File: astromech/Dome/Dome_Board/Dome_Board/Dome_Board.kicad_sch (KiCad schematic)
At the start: 3 parts, among them J1 Conn_01x02_Socket, J2 Conn_01x02_Socket, U1 ESP32-C6-DEVKITC-1-N8

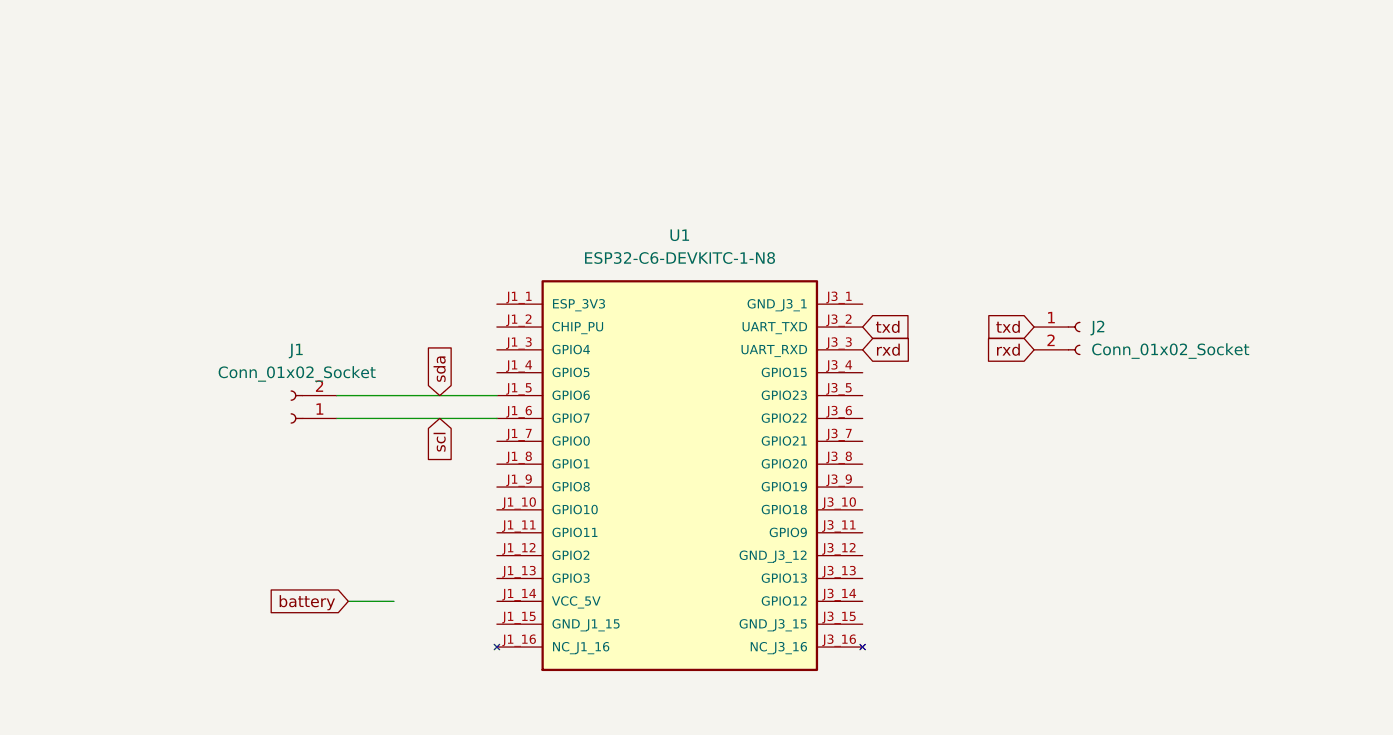
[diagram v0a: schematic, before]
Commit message: added battery 5vRegulator 10/12
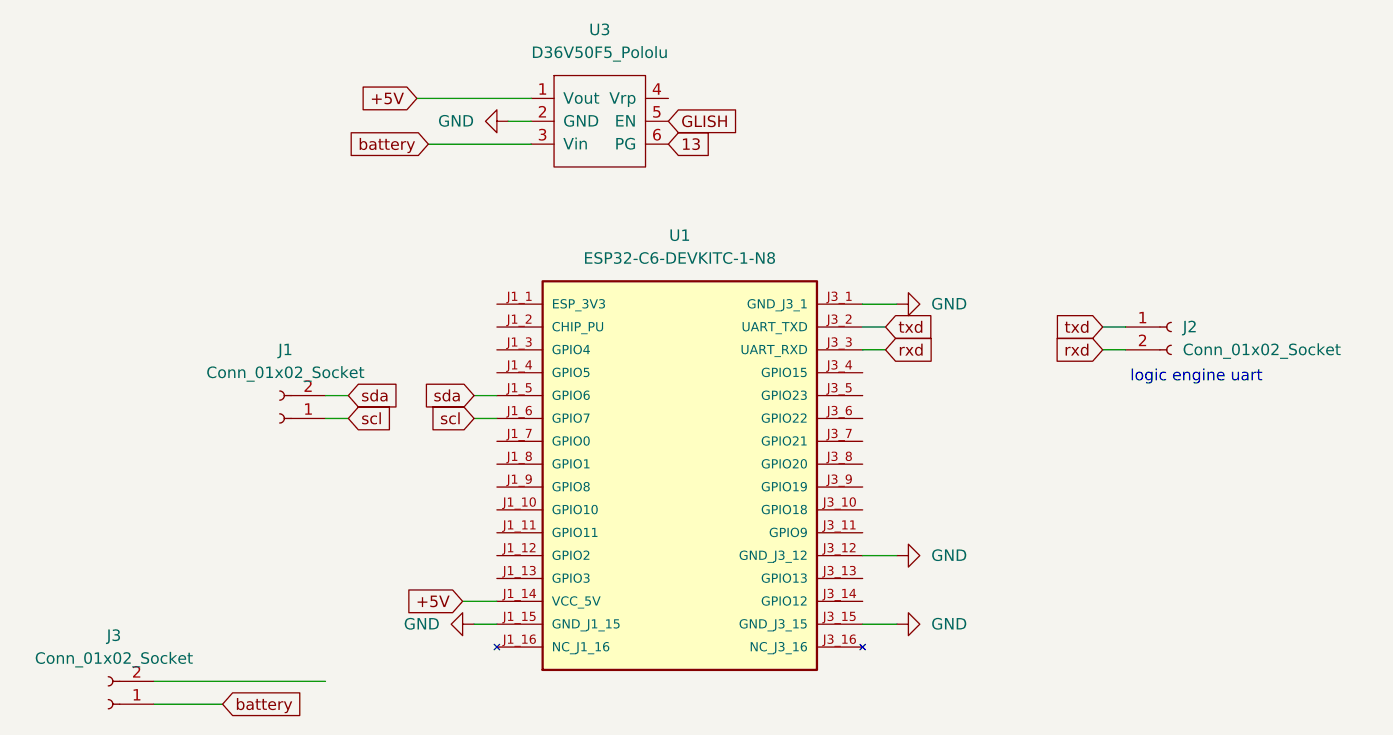
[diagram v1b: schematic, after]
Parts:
- added J3: Conn_01x02_Socket, Connector_PinSocket_1.27mm:PinSocket_1x02_P1.27mm_Vertical, symbol Connector:Conn_01x02_Socket
- added U3: D36V50F5_Pololu, js:D36V50F5_Pololu, symbol js:D36V50F5_Pololu
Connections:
- net battery: now also J3.1 (Pin_1), U3.3 (Vin)
- net +5V: now reaches U1.J1_14 (VCC_5V)
- net +5V: now also U3.1 (Vout)
- net GND: now reaches U1.J1_15 (GND_J1_15)
- net GND: now also U1.J3_1 (GND_J3_1), U1.J3_12 (GND_J3_12), U1.J3_15 (GND_J3_15), U3.2 (GND)
- new net 13: U3.6 (PG)
- new net GLISH: U3.5 (EN)
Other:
- note added: "logic engine uart"
- moved on the sheet: J1, J2

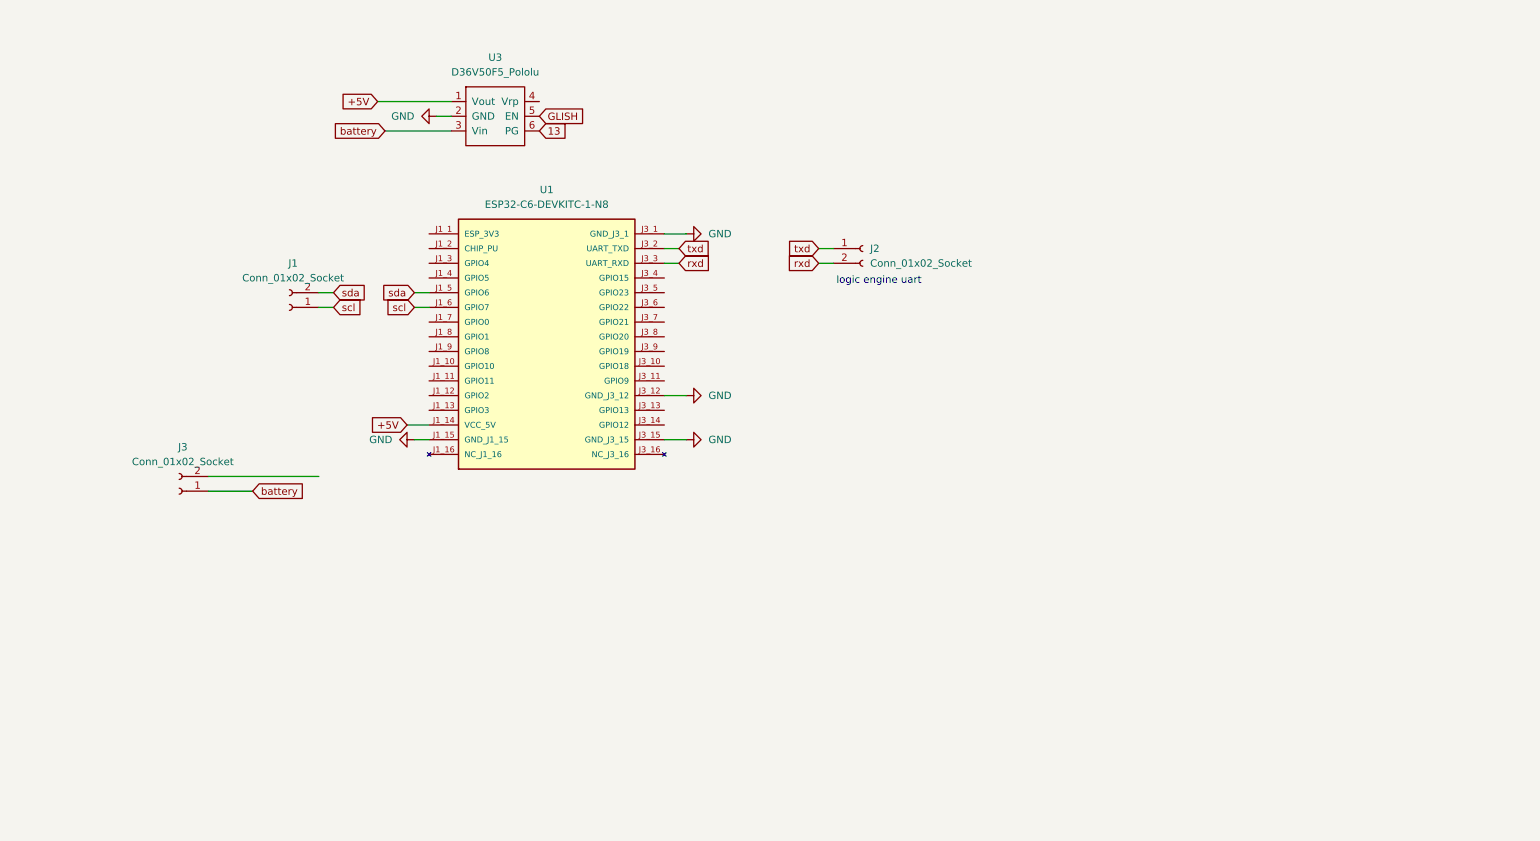
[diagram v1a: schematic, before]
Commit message: added txd lp, rxd lp, pwd connectors
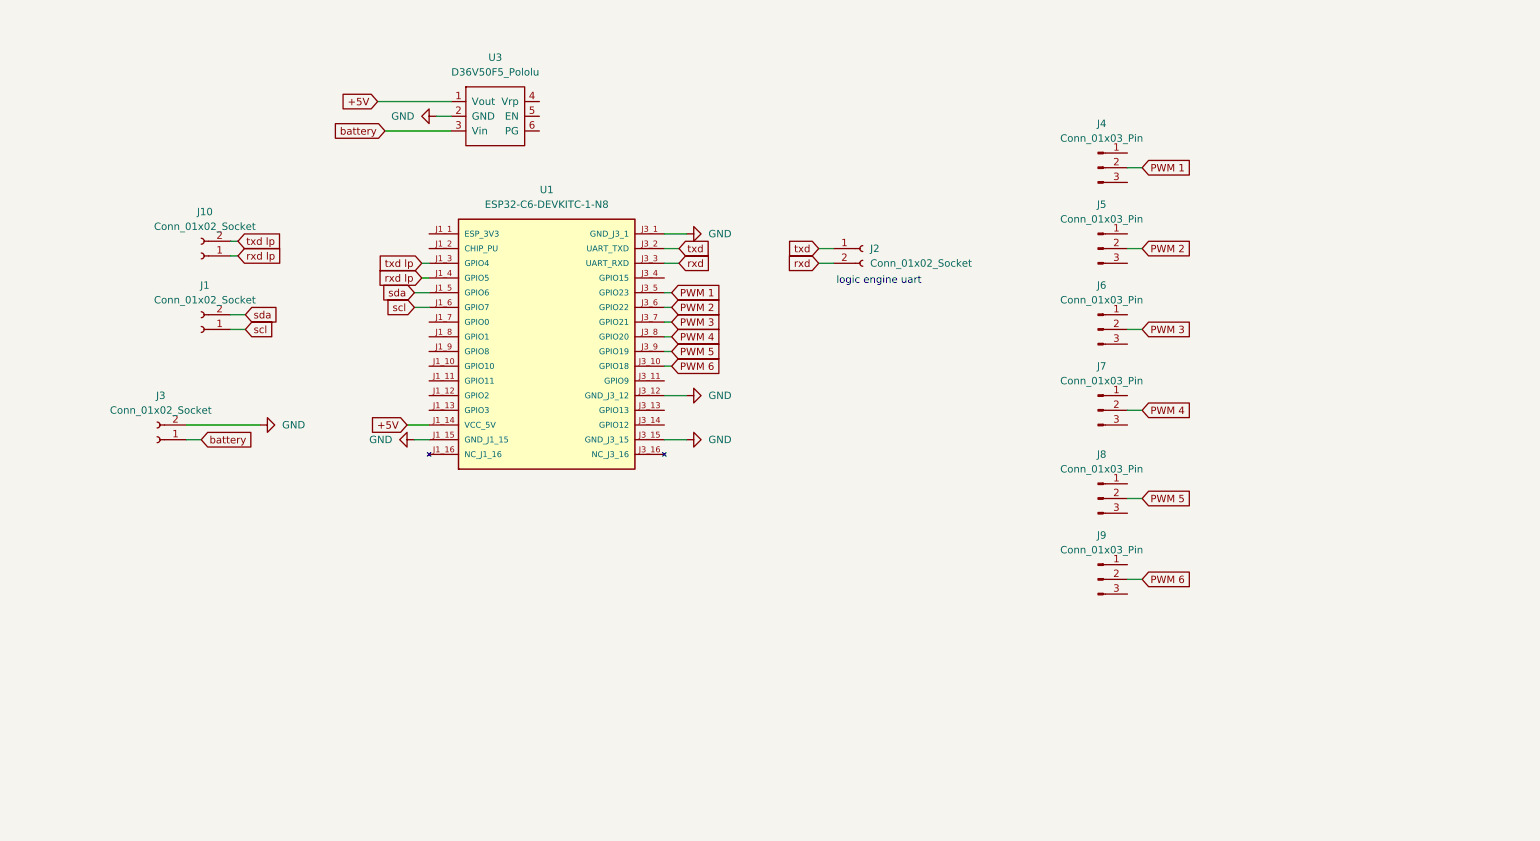
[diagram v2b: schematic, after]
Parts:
- added J10: Conn_01x02_Socket, Connector_PinSocket_1.27mm:PinSocket_1x02_P1.27mm_Vertical, symbol Connector:Conn_01x02_Socket
- added J4, J5, J6, J7, J8, J9: Conn_01x03_Pin, Connector_PinHeader_2.54mm:PinHeader_1x03_P2.54mm_Vertical, symbol Connector:Conn_01x03_Pin
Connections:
- net GND: now also J3.2 (Pin_2)
- net txd lp: now reaches U1.J1_3 (GPIO4)
- net txd lp: now also J10.2 (Pin_2)
- net rxd lp: now reaches U1.J1_4 (GPIO5)
- net rxd lp: now also J10.1 (Pin_1)
- net PWM 6: now reaches U1.J3_10 (GPIO18)
- net PWM 6: now also J9.2 (Pin_2)
- net PWM 1: now reaches U1.J3_5 (GPIO23)
- net PWM 1: now also J4.2 (Pin_2)
- net PWM 2: now reaches U1.J3_6 (GPIO22)
- net PWM 2: now also J5.2 (Pin_2)
- net PWM 3: now reaches U1.J3_7 (GPIO21)
- net PWM 3: now also J6.2 (Pin_2)
- net PWM 4: now reaches U1.J3_8 (GPIO20)
- net PWM 4: now also J7.2 (Pin_2)
- net PWM 5: now reaches U1.J3_9 (GPIO19)
- net PWM 5: now also J8.2 (Pin_2)
- net 13: no longer names the net of U3.6 (PG)
- net GLISH: no longer names the net of U3.5 (EN)
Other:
- moved on the sheet: J1, J3

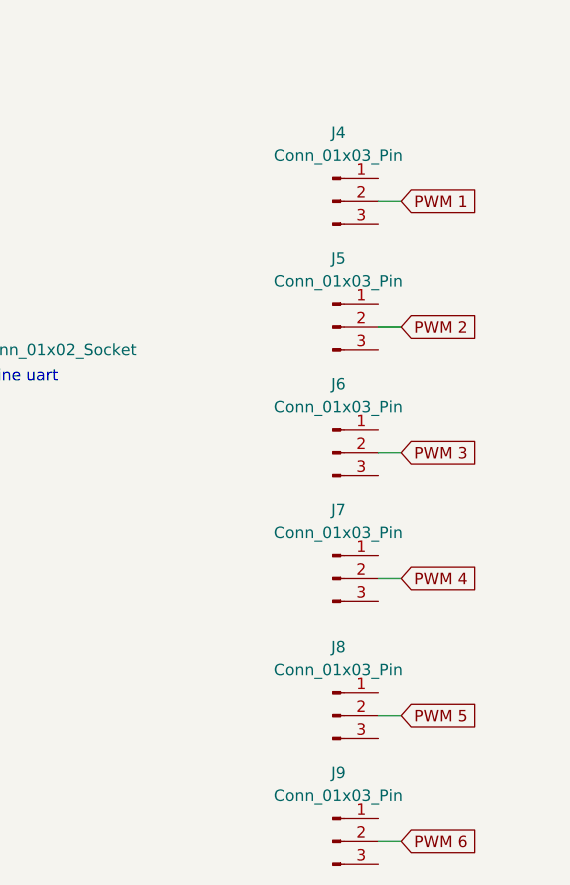
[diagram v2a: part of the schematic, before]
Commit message: added txd lp, rxd lp, PWM connectors
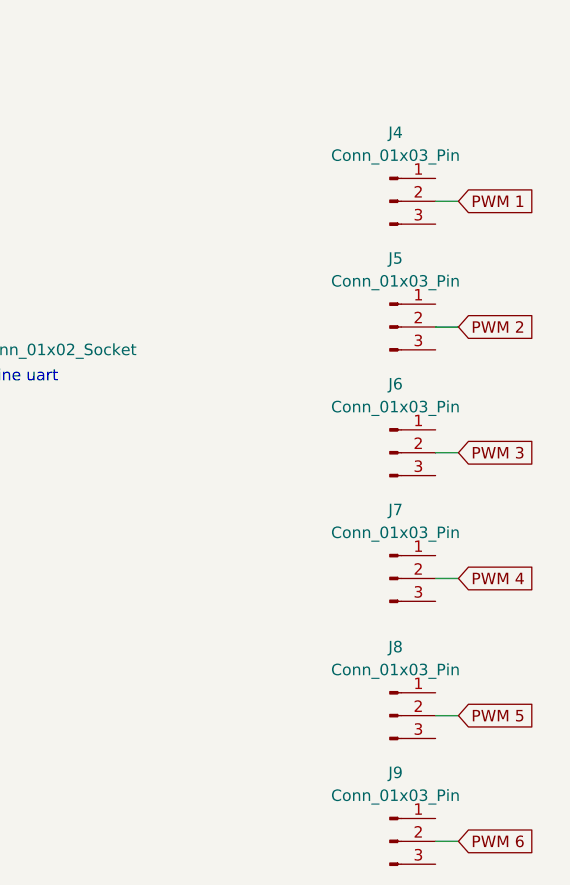
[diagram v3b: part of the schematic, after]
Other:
- moved on the sheet: J4, J5, J6, J7, J8, J9
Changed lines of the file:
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@@
 	(wire
 		(pts
-			(xy 209.55 100.33) (xy 207.01 100.33)
+			(xy 215.9 100.33) (xy 213.36 100.33)
 		)
 		(stroke
@@
 	(wire
 		(pts
-			(xy 209.55 71.12) (xy 207.01 71.12)
+			(xy 215.9 71.12) (xy 213.36 71.12)
 		)
 		(stroke
@@
 	(wire
 		(pts
-			(xy 209.55 57.15) (xy 207.01 57.15)
+			(xy 215.9 57.15) (xy 213.36 57.15)
 		)
 		(stroke
@@
 	(wire
 		(pts
-			(xy 209.55 43.18) (xy 207.01 43.18)
+			(xy 215.9 43.18) (xy 213.36 43.18)
 		)
 		(stroke
@@
 	(wire
 		(pts
-			(xy 209.55 85.09) (xy 207.01 85.09)
+			(xy 215.9 85.09) (xy 213.36 85.09)
 		)
 		(stroke
@@
 	(wire
 		(pts
-			(xy 209.55 114.3) (xy 207.01 114.3)
+			(xy 215.9 114.3) (xy 213.36 114.3)
 		)
 		(stroke
@@
 	(global_label "PWM 4"
 		(shape input)
-		(at 209.55 85.09 0)
+		(at 215.9 85.09 0)
 		(fields_autoplaced yes)
 		(effects
@@
 		)
 		(property "Intersheetrefs" "${INTERSHEET_REFS}"
-			(at 218.8851 85.09 0)
+			(at 225.2351 85.09 0)
 			(effects
 				(font
@@
 	(global_label "PWM 2"
 		(shape input)
-		(at 209.55 57.15 0)
+		(at 215.9 57.15 0)
 		(fields_autoplaced yes)
 		(effects
@@
 		)
 		(property "Intersheetrefs" "${INTERSHEET_REFS}"
-			(at 218.8851 57.15 0)
+			(at 225.2351 57.15 0)
 			(effects
 				(font
@@
 	(global_label "PWM 6"
 		(shape input)
-		(at 209.55 114.3 0)
+		(at 215.9 114.3 0)
 		(fields_autoplaced yes)
 		(effects
@@
 		)
 		(property "Intersheetrefs" "${INTERSHEET_REFS}"
-			(at 218.8851 114.3 0)
+			(at 225.2351 114.3 0)
 			(effects
 				(font
@@
 	(global_label "PWM 1"
 		(shape input)
-		(at 209.55 43.18 0)
+		(at 215.9 43.18 0)
 		(fields_autoplaced yes)
 		(effects
@@
 		)
 		(property "Intersheetrefs" "${INTERSHEET_REFS}"
-			(at 221.1228 43.18 0)
+			(at 227.4728 43.18 0)
 			(effects
 				(font
@@
 	(global_label "PWM 3"
 		(shape input)
-		(at 209.55 71.12 0)
+		(at 215.9 71.12 0)
 		(fields_autoplaced yes)
 		(effects
@@
 		)
 		(property "Intersheetrefs" "${INTERSHEET_REFS}"
-			(at 218.8851 71.12 0)
+			(at 225.2351 71.12 0)
 			(effects
 				(font
@@
 	(global_label "PWM 5"
 		(shape input)
-		(at 209.55 100.33 0)
+		(at 215.9 100.33 0)
 		(fields_autoplaced yes)
 		(effects
@@
 		)
 		(property "Intersheetrefs" "${INTERSHEET_REFS}"
-			(at 218.8851 100.33 0)
+			(at 225.2351 100.33 0)
 			(effects
 				(font
@@
 	(symbol
 		(lib_id "Connector:Conn_01x03_Pin")
-		(at 201.93 57.15 0)
+		(at 208.28 57.15 0)
 		(unit 1)
 		(exclude_from_sim no)
@@
 		(fields_autoplaced yes)
 		(property "Reference" "J5"
-			(at 202.565 49.53 0)
+			(at 208.915 49.53 0)
 			(effects
 				(font
@@
 		)
 		(property "Value" "Conn_01x03_Pin"
-			(at 202.565 52.07 0)
+			(at 208.915 52.07 0)
 			(effects
 				(font
@@
 		)
 		(property "Footprint" "Connector_PinHeader_2.54mm:PinHeader_1x03_P2.54mm_Vertical"
-			(at 201.93 57.15 0)
+			(at 208.28 57.15 0)
 			(effects
 				(font
@@
 		)
 		(property "Datasheet" "~"
-			(at 201.93 57.15 0)
+			(at 208.28 57.15 0)
 			(effects
 				(font
@@
 		)
 		(property "Description" "Generic connector, single row, 01x03, script generated"
-			(at 201.93 57.15 0)
+			(at 208.28 57.15 0)
 			(effects
 				(font
@@
 	(symbol
 		(lib_id "Connector:Conn_01x03_Pin")
-		(at 201.93 100.33 0)
+		(at 208.28 100.33 0)
 		(unit 1)
 		(exclude_from_sim no)
@@
 		(fields_autoplaced yes)
 		(property "Reference" "J8"
-			(at 202.565 92.71 0)
+			(at 208.915 92.71 0)
 			(effects
 				(font
@@
 		)
 		(property "Value" "Conn_01x03_Pin"
-			(at 202.565 95.25 0)
+			(at 208.915 95.25 0)
 			(effects
 				(font
@@
 		)
 		(property "Footprint" "Connector_PinHeader_2.54mm:PinHeader_1x03_P2.54mm_Vertical"
-			(at 201.93 100.33 0)
+			(at 208.28 100.33 0)
 			(effects
 				(font
@@
 		)
 		(property "Datasheet" "~"
-			(at 201.93 100.33 0)
+			(at 208.28 100.33 0)
 			(effects
 				(font
@@
 		)
 		(property "Description" "Generic connector, single row, 01x03, script generated"
-			(at 201.93 100.33 0)
+			(at 208.28 100.33 0)
 			(effects
 				(font
@@
 	(symbol
 		(lib_id "Connector:Conn_01x03_Pin")
-		(at 201.93 43.18 0)
+		(at 208.28 43.18 0)
 		(unit 1)
 		(exclude_from_sim no)
@@
 		(fields_autoplaced yes)
 		(property "Reference" "J4"
-			(at 202.565 35.56 0)
+			(at 208.915 35.56 0)
 			(effects
 				(font
@@
 		)
 		(property "Value" "Conn_01x03_Pin"
-			(at 202.565 38.1 0)
+			(at 208.915 38.1 0)
 			(effects
 				(font
@@
 		)
 		(property "Footprint" "Connector_PinHeader_2.54mm:PinHeader_1x03_P2.54mm_Vertical"
-			(at 201.93 43.18 0)
+			(at 208.28 43.18 0)
 			(effects
 				(font
@@
 		)
 		(property "Datasheet" "~"
-			(at 201.93 43.18 0)
+			(at 208.28 43.18 0)
 			(effects
 				(font
@@
 		)
 		(property "Description" "Generic connector, single row, 01x03, script generated"
-			(at 201.93 43.18 0)
+			(at 208.28 43.18 0)
 			(effects
 				(font
@@
 	(symbol
 		(lib_id "Connector:Conn_01x03_Pin")
-		(at 201.93 114.3 0)
+		(at 208.28 114.3 0)
 		(unit 1)
 		(exclude_from_sim no)
@@
 		(fields_autoplaced yes)
 		(property "Reference" "J9"
-			(at 202.565 106.68 0)
+			(at 208.915 106.68 0)
 			(effects
 				(font
@@
 		)
 		(property "Value" "Conn_01x03_Pin"
-			(at 202.565 109.22 0)
+			(at 208.915 109.22 0)
 			(effects
 				(font
@@
 		)
 		(property "Footprint" "Connector_PinHeader_2.54mm:PinHeader_1x03_P2.54mm_Vertical"
-			(at 201.93 114.3 0)
+			(at 208.28 114.3 0)
 			(effects
 				(font
@@
 		)
 		(property "Datasheet" "~"
-			(at 201.93 114.3 0)
+			(at 208.28 114.3 0)
 			(effects
 				(font
@@
 		)
 		(property "Description" "Generic connector, single row, 01x03, script generated"
-			(at 201.93 114.3 0)
+			(at 208.28 114.3 0)
 			(effects
 				(font
@@
 	(symbol
 		(lib_id "Connector:Conn_01x03_Pin")
-		(at 201.93 85.09 0)
+		(at 208.28 85.09 0)
 		(unit 1)
 		(exclude_from_sim no)
@@
 		(fields_autoplaced yes)
 		(property "Reference" "J7"
-			(at 202.565 77.47 0)
+			(at 208.915 77.47 0)
 			(effects
 				(font
@@
 		)
 		(property "Value" "Conn_01x03_Pin"
-			(at 202.565 80.01 0)
+			(at 208.915 80.01 0)
 			(effects
 				(font
@@
 		)
 		(property "Footprint" "Connector_PinHeader_2.54mm:PinHeader_1x03_P2.54mm_Vertical"
-			(at 201.93 85.09 0)
+			(at 208.28 85.09 0)
 			(effects
 				(font
@@
 		)
 		(property "Datasheet" "~"
-			(at 201.93 85.09 0)
+			(at 208.28 85.09 0)
 			(effects
 				(font
@@
 		)
 		(property "Description" "Generic connector, single row, 01x03, script generated"
-			(at 201.93 85.09 0)
+			(at 208.28 85.09 0)
 			(effects
 				(font
@@
 	(symbol
 		(lib_id "Connector:Conn_01x03_Pin")
-		(at 201.93 71.12 0)
+		(at 208.28 71.12 0)
 		(unit 1)
 		(exclude_from_sim no)
@@
 		(fields_autoplaced yes)
 		(property "Reference" "J6"
-			(at 202.565 63.5 0)
+			(at 208.915 63.5 0)
 			(effects
 				(font
@@
 		)
 		(property "Value" "Conn_01x03_Pin"
-			(at 202.565 66.04 0)
+			(at 208.915 66.04 0)
 			(effects
 				(font
@@
 		)
 		(property "Footprint" "Connector_PinHeader_2.54mm:PinHeader_1x03_P2.54mm_Vertical"
-			(at 201.93 71.12 0)
+			(at 208.28 71.12 0)
 			(effects
 				(font
@@
 		)
 		(property "Datasheet" "~"
-			(at 201.93 71.12 0)
+			(at 208.28 71.12 0)
 			(effects
 				(font
@@
 		)
 		(property "Description" "Generic connector, single row, 01x03, script generated"
-			(at 201.93 71.12 0)
-			(effects
-				(font
+			(at 208.28 71.12 0)
+			(effects
+				(font

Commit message: added low power txd, low power rxd, PWM connectors
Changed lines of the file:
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@@
+	(symbol
+		(lib_id "power:GND")
+		(at 59.69 101.6 90)
+		(unit 1)
+		(exclude_from_sim no)
+		(in_bom yes)
+		(on_board yes)
+		(dnp no)
+		(fields_autoplaced yes)
+		(property "Reference" "#PWR07"
+			(at 66.04 101.6 0)
+			(effects
+				(font
+					(size 1.27 1.27)
+				)
+				(hide yes)
+			)
+		)
+		(property "Value" "GND"
+			(at 63.5 101.5999 90)
+			(effects
+				(font
+					(size 1.27 1.27)
+				)
+				(justify right)
+			)
+		)
+		(property "Footprint" ""
+			(at 59.69 101.6 0)
+			(effects
+				(font
+					(size 1.27 1.27)
+				)
+				(hide yes)
+			)
+		)
+		(property "Datasheet" ""
+			(at 59.69 101.6 0)
+			(effects
+				(font
+					(size 1.27 1.27)
+				)
+				(hide yes)
+			)
+		)
+		(property "Description" "Power symbol creates a global label with name \"GND\" , ground"
+			(at 59.69 101.6 0)
+			(effects
+				(font
+					(size 1.27 1.27)
+				)
+				(hide yes)
+			)
+		)
+		(pin "1"
+		)
+		(instances
+			(project "Dome_Board"
+				(path "/90e17e97-00aa-43db-9ad2-331febdc7c45"
+					(reference "#PWR07")
+					(unit 1)
+				)
+			)
+		)
+	)
 	(symbol
 		(lib_id "power:GND")
